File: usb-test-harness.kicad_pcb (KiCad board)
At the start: 4 copper layers, 98 x 85 mm, 88 parts, among them J1 5V_RAW, J10 USB_A_DUAL, J2 GND, J3 V_EXT, J4 USB_A (female down), J5 Conn_01x03_Male, J6 USB_A_DUAL, J7 USB_A_DUAL, J8 USB_A SOFNG USB-05, J9 USB_B_Micro (up), U1 FT24C02A, U2 SE5120ST33, U3 USB2517, U4 APL3511C, U5 APL3511C, U6 APL3511C, U7 APL3511C, U8 APL3511C, U9 APL3511C, Y1 24MHz

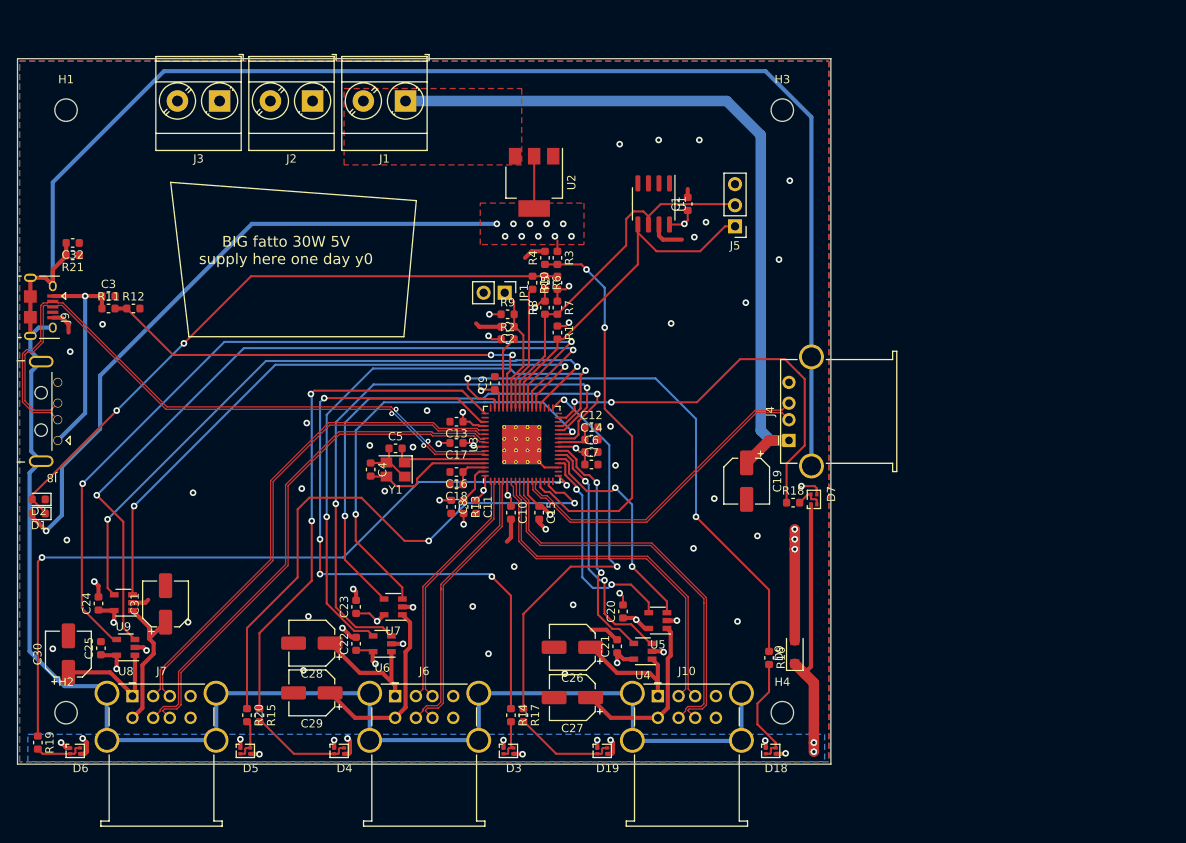
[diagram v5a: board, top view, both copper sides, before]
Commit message: usb-hub: tidy up lots of silk
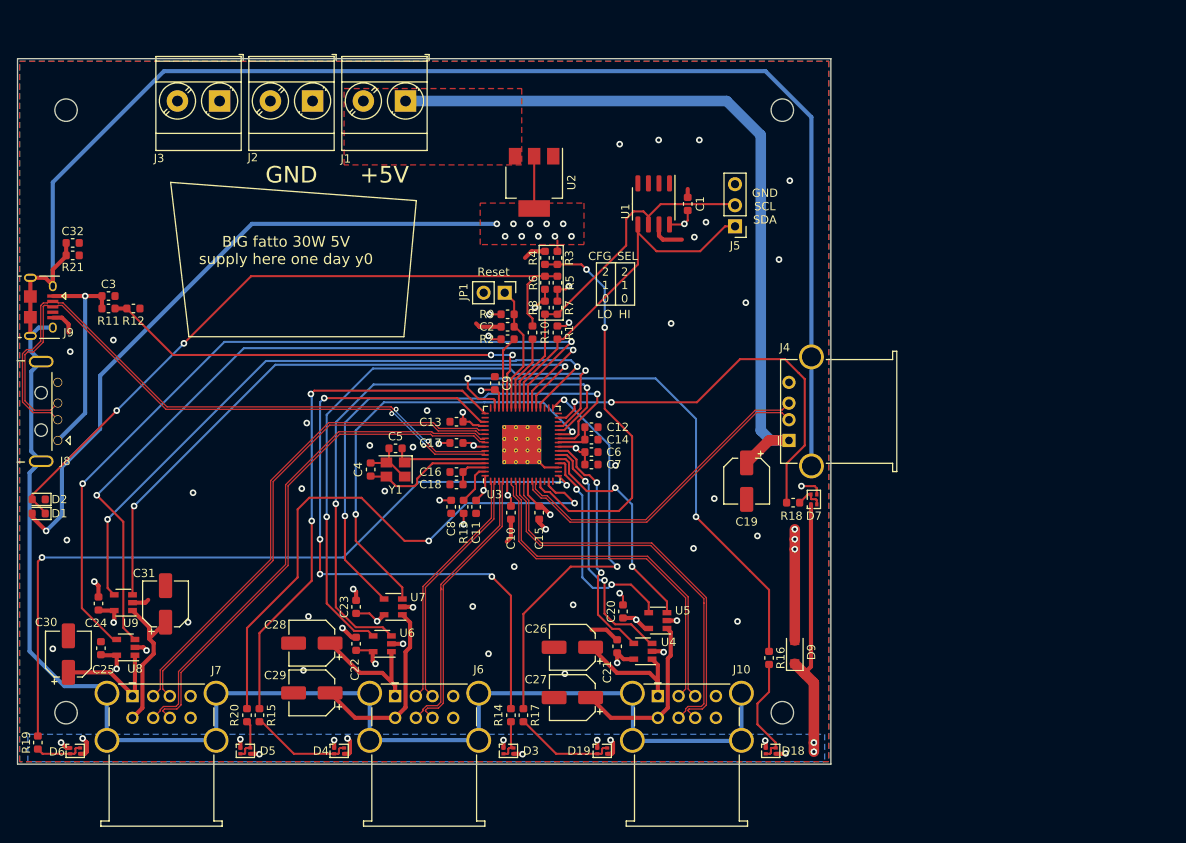
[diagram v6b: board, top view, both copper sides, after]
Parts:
- moved R10 6.00 mm to (161.3, 83.6)
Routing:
- net /upstream-config-leds/CFG_SEL1: track 77.1 -> 83.3 mm
- net /upstream-config-leds/CFG_SEL1_A: track 15.1 -> 9.15 mm
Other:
- board text added: "+5V"
- board text added: "2 1 0"
- board text added: "CFG_SEL"
- board text added: "FIX ALL THE FUCKING SILK!"
- board text added: "GND"
- board text added: "GND SCL SDA"
- board text added: "HI"
- board text added: "LO"
- board text added: "Reset"

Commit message: updates: bits
* add in/out caps on 3v3 supply (how was that missed?)
* switch to pluggable terminal blocks.  better forr case design, better
  for humans, ~same price
* added more notes on suitable esd protection on usb
* still no input protection on 5v.
* Added the stupid mounting hole that ruins it all with the current
  chosen case.
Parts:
- removed J2: GND, TerminalBlock_Phoenix:TerminalBlock_Phoenix_MKDS-3-2-5.08_1x02_P5.08mm_Horizontal
- removed J3: V_EXT, TerminalBlock_Phoenix:TerminalBlock_Phoenix_MKDS-3-2-5.08_1x02_P5.08mm_Horizontal
- added C33: 10uF, Capacitor_SMD:C_0603_1608Metric, F.Cu at (160.0, 59.8)
- added C34: 10uF, Capacitor_SMD:C_0603_1608Metric, F.Cu at (166.5, 68.0)
- added H5: MountingHole, MountingHole:MountingHole_4mm, F.Cu at (227.3, 93.2)
- added U10: NUP4202, Package_TO_SOT_SMD:SOT-363_SC-70-6, F.Cu at (232.0, 109.5)
- added U11: NUP4202, Package_TO_SOT_SMD:SOT-363_SC-70-6, F.Cu at (232.0, 113.3)
- added U12: NUP4202, Package_TO_SOT_SMD:SOT-363_SC-70-6, F.Cu at (236.3, 109.5)
- J1: value 5V_RAW -> Conn_01x06; footprint TerminalBlock_Phoenix:TerminalBlock_Phoenix_MKDS-3-2-5.08_1x02_P5.08mm_Horizontal -> Connector_Phoenix_MSTB:PhoenixContact_MSTBA_2,5_6-G-5,08_1x06_P5.08mm_Horizontal
- J8: value USB_A SOFNG USB-05 -> USB_A male UP
- U1: value FT24C02A -> 2k i2c eeprom
